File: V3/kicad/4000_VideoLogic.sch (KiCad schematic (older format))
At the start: 0 parts

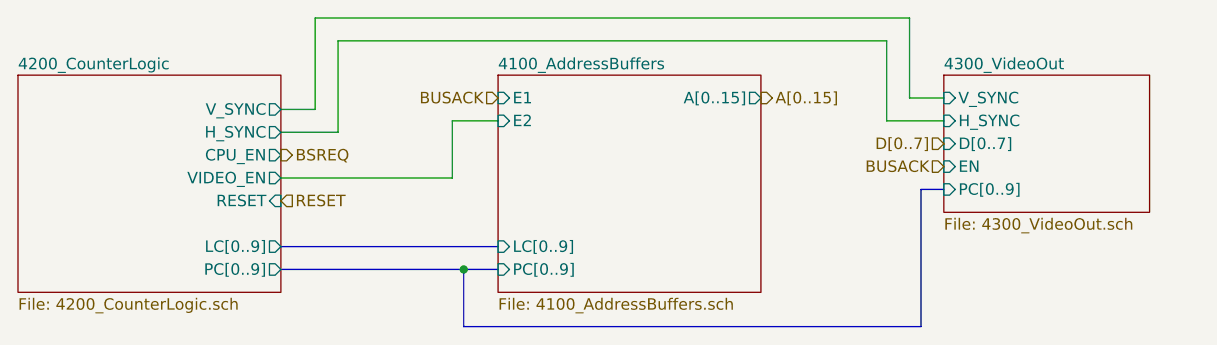
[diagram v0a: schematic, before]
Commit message: probably going to split into two boards
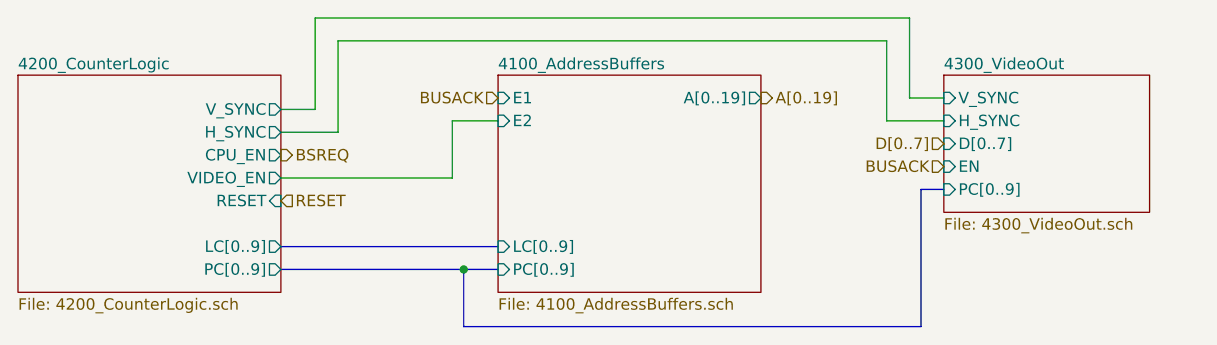
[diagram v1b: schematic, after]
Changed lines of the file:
@@
 $Descr A4 11693 8268
 encoding utf-8
-Sheet 12 16
+Sheet 6 10
 Title ""
 Date ""
@@
 F2 "E1" I L 5400 3350 50
 F3 "E2" I L 5400 3450 50
-F4 "A[0..15]" O R 6550 3350 50
-F5 "LC[0..9]" I L 5400 4000 50
-F6 "PC[0..9]" I L 5400 4100 50
+F4 "LC[0..9]" I L 5400 4000 50
+F5 "PC[0..9]" I L 5400 4100 50
+F6 "A[0..19]" O R 6550 3350 50
 $EndSheet
 Text HLabel 4450 3800 2    50   Input ~ 0
@@
 Text HLabel 7350 3650 0    50   Input ~ 0
 BUSACK
-Text HLabel 6550 3350 2    50   Output ~ 0
-A[0..15]
 Text HLabel 5400 3350 0    50   Input ~ 0
 BUSACK
@@
 Text HLabel 4450 3600 2    50   Output ~ 0
 BSREQ
+Text HLabel 6550 3350 2    50   Output ~ 0
+A[0..19]
 $EndSCHEMATC
